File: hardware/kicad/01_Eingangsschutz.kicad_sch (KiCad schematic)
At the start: 0 parts

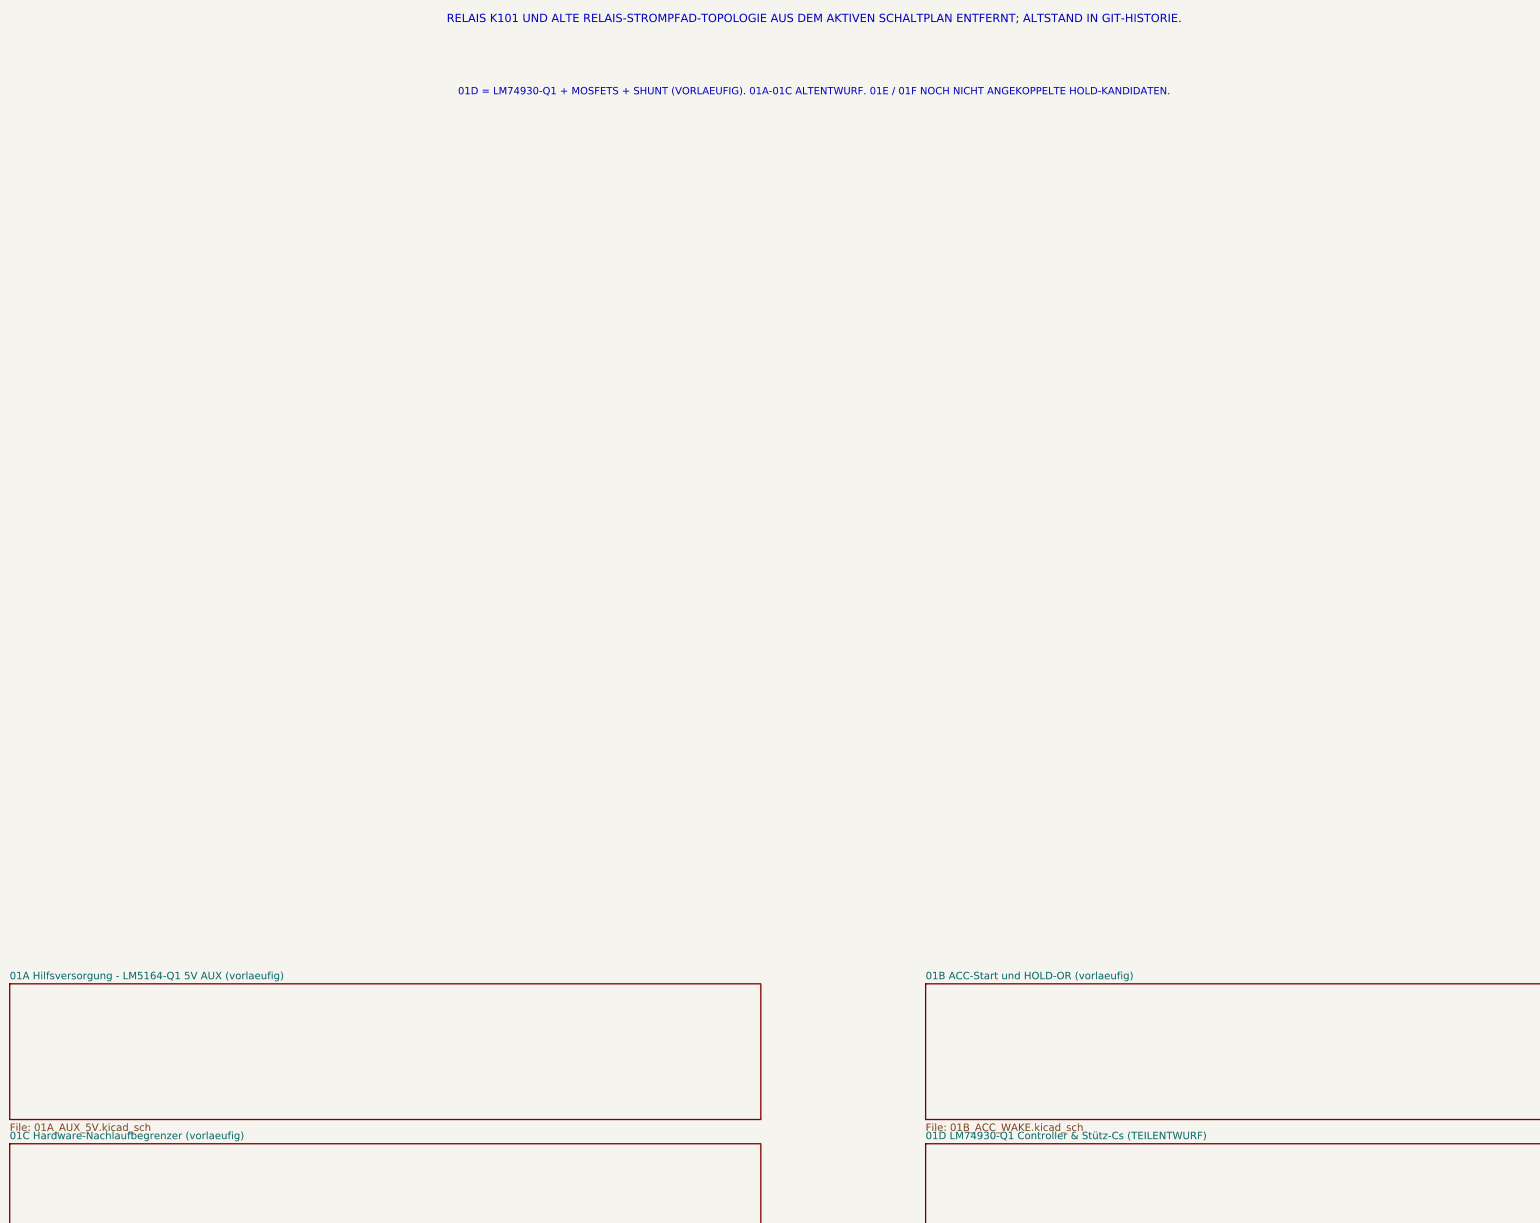
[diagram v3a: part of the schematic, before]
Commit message: hardware(power): retire redundant relay-only LM5164 auxiliary 5V sheet from active KiCad hierarchy
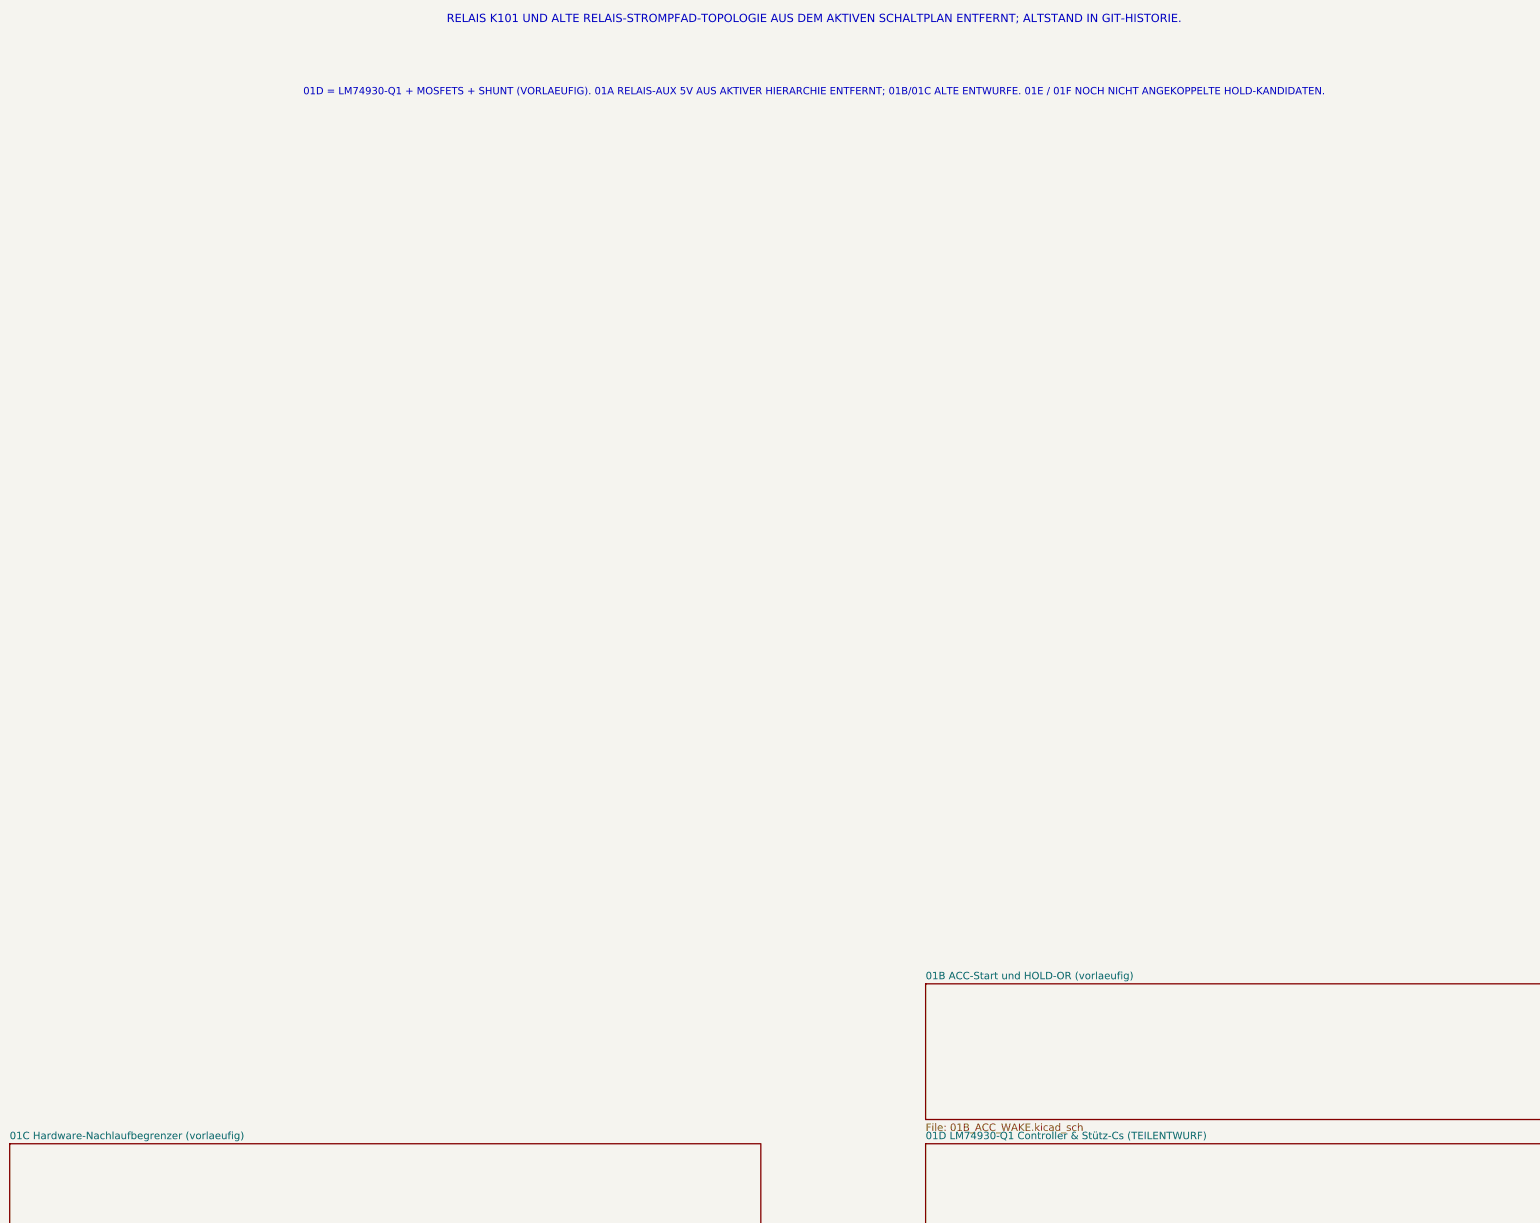
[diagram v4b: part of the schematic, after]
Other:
- removed sheet 01A Hilfsversorgung - LM5164-Q1 5V AUX (vorlaeufig)
- note added: "01D = LM74930-Q1 + MOSFETS + SHUNT (VORLAEUFIG). 01A RELAIS-AUX 5V AUS AKTIVER HIERARCHIE ENTFERNT; 01B/01C ALTE ENTWURFE. 01E / 01F NOCH NICHT ANGEKOPPELTE HOLD-KANDIDATEN."
- note removed: "01D = LM74930-Q1 + MOSFETS + SHUNT (VORLAEUFIG). 01A-01C ALTENTWURF. 01E / 01F NOCH NICHT ANGEKOPPELTE HOLD-KANDIDATEN."
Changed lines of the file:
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@@
 (kicad_sch (version 20250114) (generator "eeschema")
 (paper "A2")
-(title_block (title "TripTracer V1 - Automotive Eingangsschutz, relayless design") (date "2026-10-14") (rev "RELAY REMOVED / LM74930+LMR36520 WIP"))
+(title_block (title "TripTracer V1 - Automotive Eingangsschutz, relayless design") (date "2026-10-14") (rev "LMR38020 MAIN BUCK / LEGACY CIRCUITS NOT APPROVED"))
 (text "RELAIS K101 UND ALTE RELAIS-STROMPFAD-TOPOLOGIE AUS DEM AKTIVEN SCHALTPLAN ENTFERNT; ALTSTAND IN GIT-HISTORIE." (at 191 58 0) (effects (font (size 1.7 1.7))))
-(text "01D = LM74930-Q1 + MOSFETS + SHUNT (VORLAEUFIG). 01A-01C ALTENTWURF. 01E / 01F NOCH NICHT ANGEKOPPELTE HOLD-KANDIDATEN." (at 191 73 0) (effects (font (size 1.5 1.5))))
-(sheet (at 25 257) (size 155 28) (exclude_from_sim no) (in_bom yes) (on_board yes) (dnp no)
- (stroke (width 0) (type solid)) (fill (color 0 0 0 0))
- (property "Sheetname" "01A Hilfsversorgung - LM5164-Q1 5V AUX (vorlaeufig)" (at 25 256.24 0) (effects (font (size 1.524 1.524)) (justify left bottom)))
- (property "Sheetfile" "01A_AUX_5V.kicad_sch" (at 25 285.76 0) (effects (font (size 1.524 1.524)) (justify left top)))
- (instances (project "TripTracer_V1" (path "/a26d9b0c-7f10-4e5a-a65f-000000000064/a26d9b0c-7f10-4e5a-a65f-000000000065" (page "2.1"))))
-)
+(text "01D = LM74930-Q1 + MOSFETS + SHUNT (VORLAEUFIG). 01A RELAIS-AUX 5V AUS AKTIVER HIERARCHIE ENTFERNT; 01B/01C ALTE ENTWURFE. 01E / 01F NOCH NICHT ANGEKOPPELTE HOLD-KANDIDATEN." (at 191 73 0) (effects (font (size 1.5 1.5))))
 (sheet (at 214 257) (size 175 28) (exclude_from_sim no) (in_bom yes) (on_board yes) (dnp no)
  (stroke (width 0) (type solid)) (fill (color 0 0 0 0))

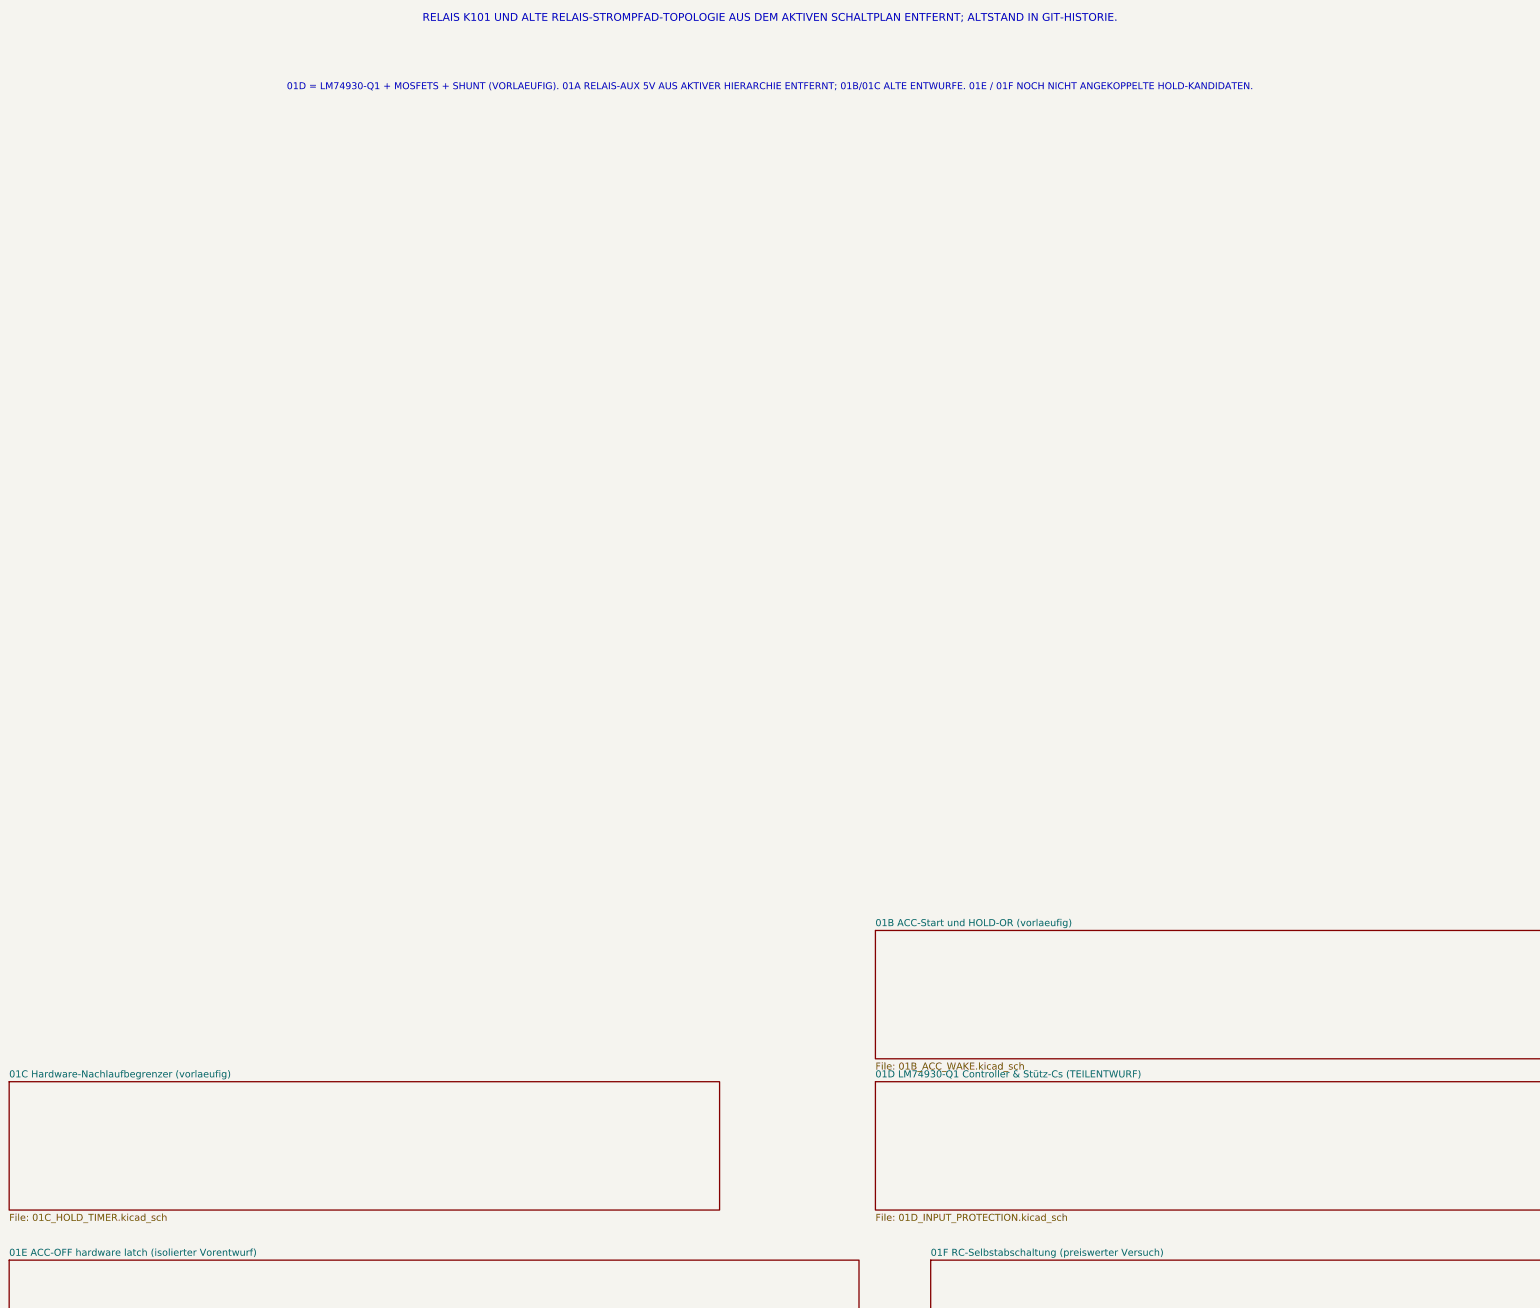
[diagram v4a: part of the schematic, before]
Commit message: hardware(input): use low-cost diode/TVS sheet instead of discontinued LM74930 in active root hierarchy
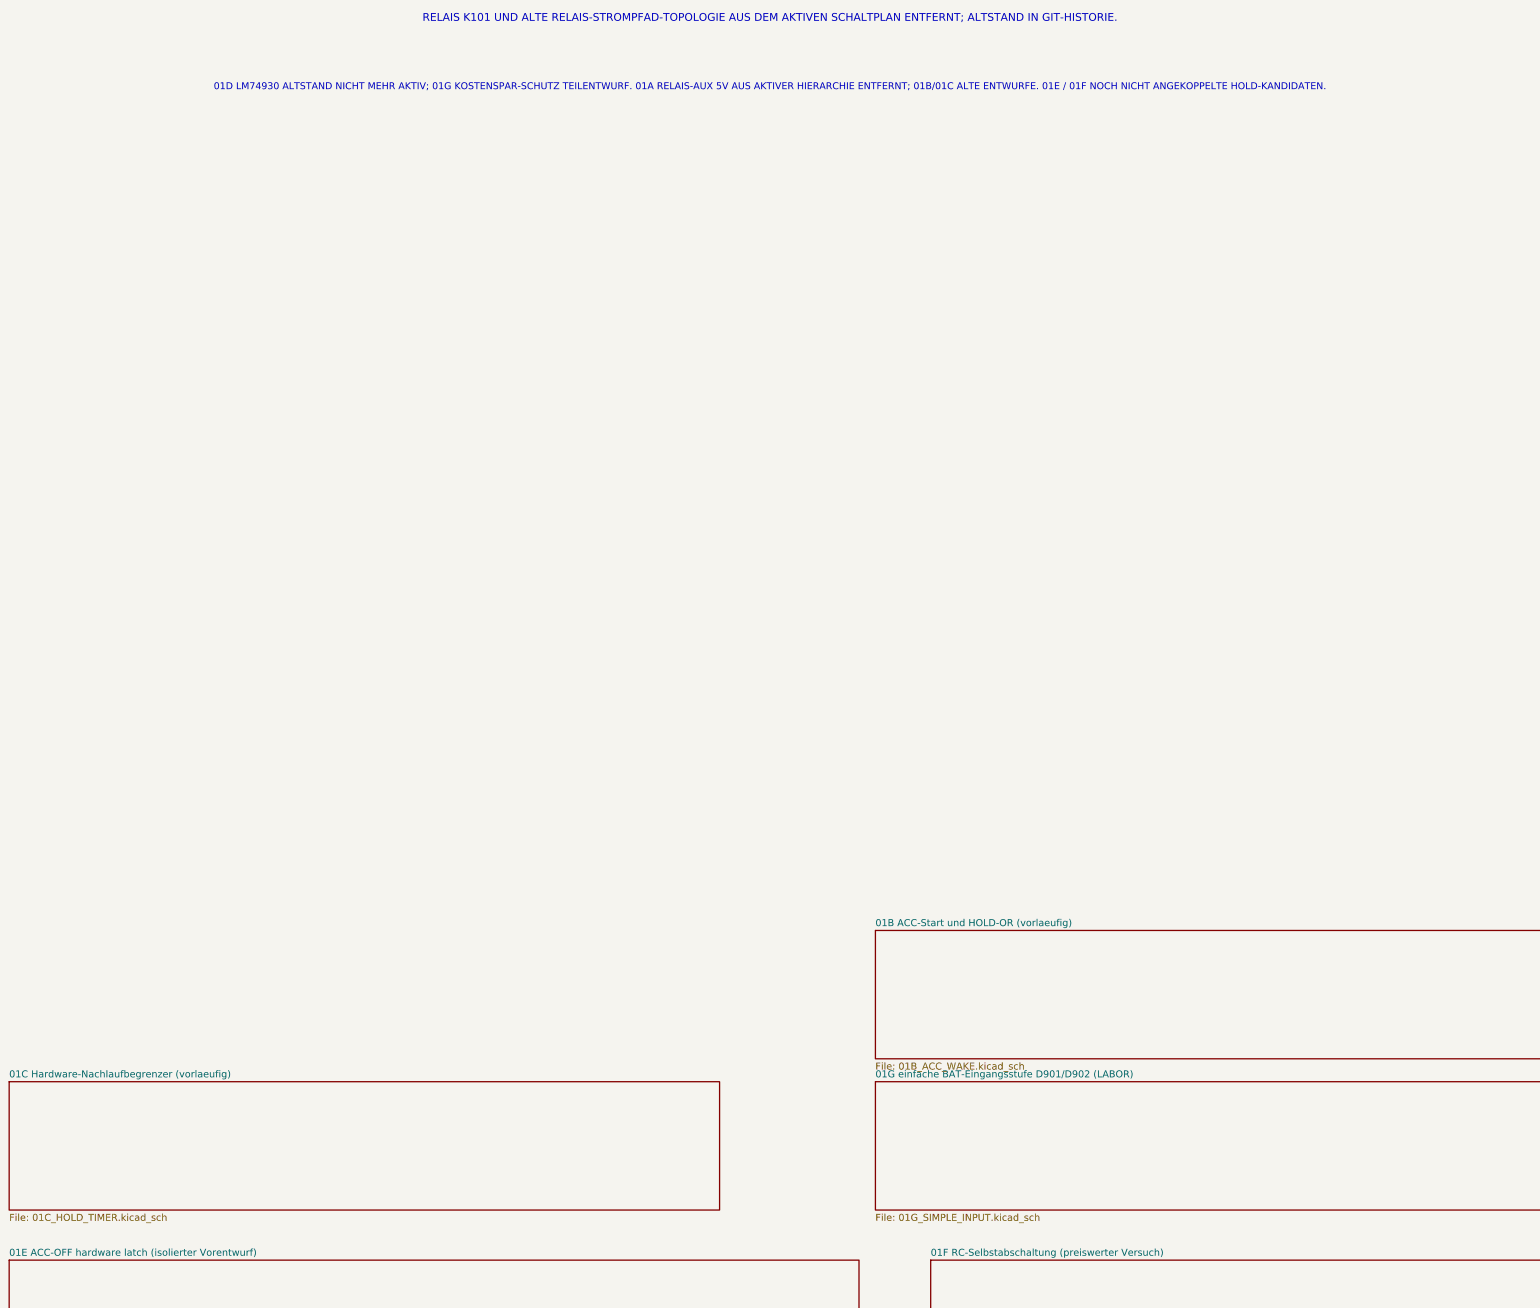
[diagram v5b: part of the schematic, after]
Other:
- sheet 01D LM74930-Q1 Controller & Stütz-Cs (TEILENTWURF) renamed 01G einfache BAT-Eingangsstufe D901/D902 (LABOR)
- sheet 01G einfache BAT-Eingangsstufe D901/D902 (LABOR): file 01D_INPUT_PROTECTION.kicad_sch -> 01G_SIMPLE_INPUT.kicad_sch
- note added: "01D LM74930 ALTSTAND NICHT MEHR AKTIV; 01G KOSTENSPAR-SCHUTZ TEILENTWURF. 01A RELAIS-AUX 5V AUS AKTIVER HIERARCHIE ENTFERNT; 01B/01C ALTE ENTWURFE. 01E / 01F NOCH NICHT ANGEKOPPELTE HOLD-KANDIDATEN."
- note removed: "01D = LM74930-Q1 + MOSFETS + SHUNT (VORLAEUFIG). 01A RELAIS-AUX 5V AUS AKTIVER HIERARCHIE ENTFERNT; 01B/01C ALTE ENTWURFE. 01E / 01F NOCH NICHT ANGEKOPPELTE HOLD-KANDIDATEN."
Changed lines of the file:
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@@
 (title_block (title "TripTracer V1 - Automotive Eingangsschutz, relayless design") (date "2026-10-14") (rev "LMR38020 MAIN BUCK / LEGACY CIRCUITS NOT APPROVED"))
 (text "RELAIS K101 UND ALTE RELAIS-STROMPFAD-TOPOLOGIE AUS DEM AKTIVEN SCHALTPLAN ENTFERNT; ALTSTAND IN GIT-HISTORIE." (at 191 58 0) (effects (font (size 1.7 1.7))))
-(text "01D = LM74930-Q1 + MOSFETS + SHUNT (VORLAEUFIG). 01A RELAIS-AUX 5V AUS AKTIVER HIERARCHIE ENTFERNT; 01B/01C ALTE ENTWURFE. 01E / 01F NOCH NICHT ANGEKOPPELTE HOLD-KANDIDATEN." (at 191 73 0) (effects (font (size 1.5 1.5))))
+(text "01D LM74930 ALTSTAND NICHT MEHR AKTIV; 01G KOSTENSPAR-SCHUTZ TEILENTWURF. 01A RELAIS-AUX 5V AUS AKTIVER HIERARCHIE ENTFERNT; 01B/01C ALTE ENTWURFE. 01E / 01F NOCH NICHT ANGEKOPPELTE HOLD-KANDIDATEN." (at 191 73 0) (effects (font (size 1.5 1.5))))
 (sheet (at 214 257) (size 175 28) (exclude_from_sim no) (in_bom yes) (on_board yes) (dnp no)
  (stroke (width 0) (type solid)) (fill (color 0 0 0 0))
@@
 (sheet (at 214 290) (size 175 28) (exclude_from_sim no) (in_bom yes) (on_board yes) (dnp no)
  (stroke (width 0) (type solid)) (fill (color 0 0 0 0))
- (property "Sheetname" "01D LM74930-Q1 Controller & Stütz-Cs (TEILENTWURF)" (at 214 289.24 0) (effects (font (size 1.524 1.524)) (justify left bottom)))
- (property "Sheetfile" "01D_INPUT_PROTECTION.kicad_sch" (at 214 318.76 0) (effects (font (size 1.524 1.524)) (justify left top)))
+ (property "Sheetname" "01G einfache BAT-Eingangsstufe D901/D902 (LABOR)" (at 214 289.24 0) (effects (font (size 1.524 1.524)) (justify left bottom)))
+ (property "Sheetfile" "01G_SIMPLE_INPUT.kicad_sch" (at 214 318.76 0) (effects (font (size 1.524 1.524)) (justify left top)))
  (instances (project "TripTracer_V1" (path "/a26d9b0c-7f10-4e5a-a65f-000000000064/a26d9b0c-7f10-4e5a-a65f-000000000065" (page "2.4"))))
 )
